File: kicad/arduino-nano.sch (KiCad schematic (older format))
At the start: 28 parts, among them J4 USB_B, J5 AVR ISP, SW5 Reset, U4 CH340C, U5 ATmega328P-AU, Y1 16MHz

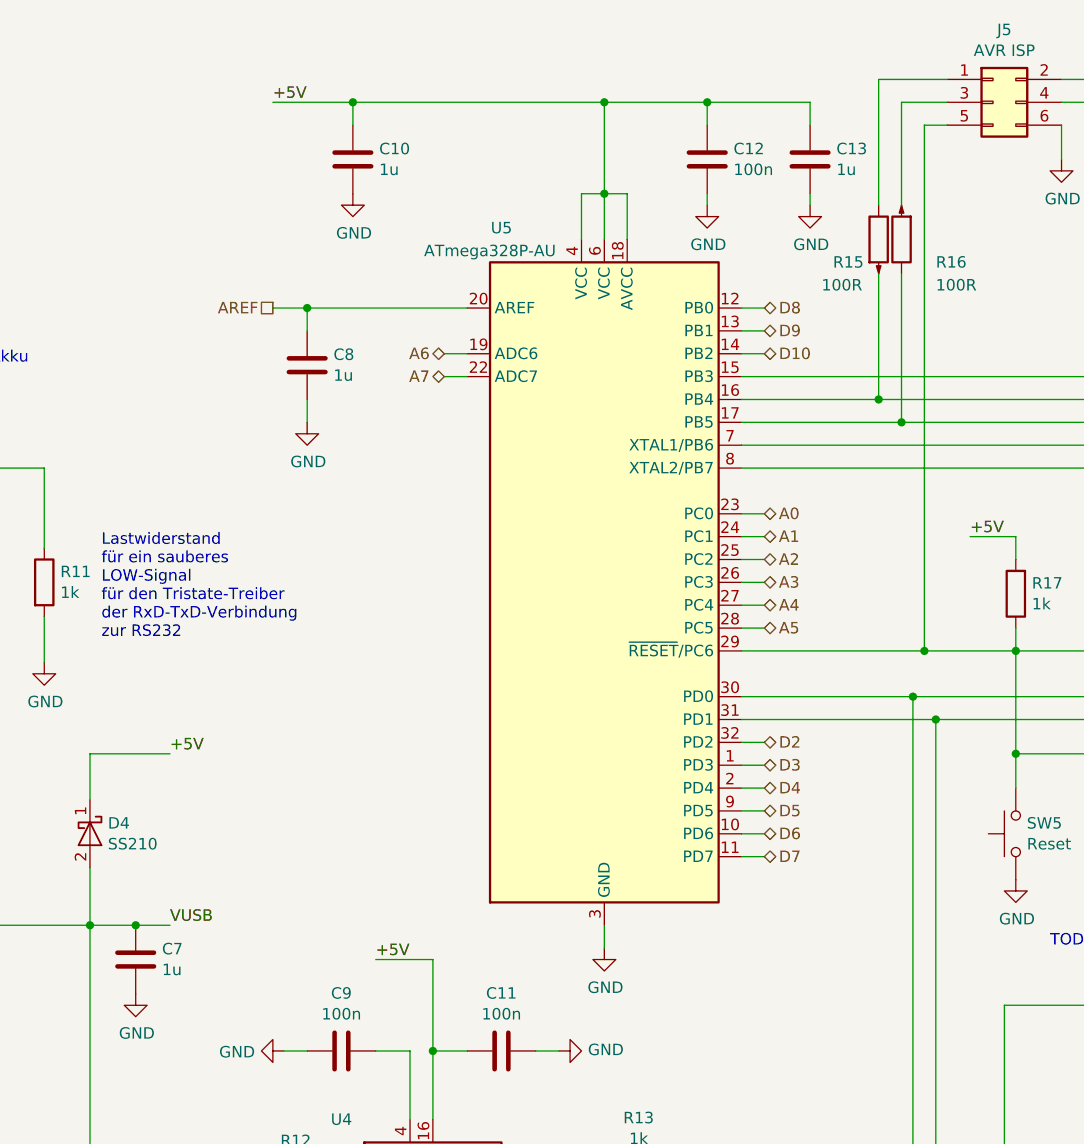
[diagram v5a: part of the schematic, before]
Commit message: wip, bugfixes für v21.0.1
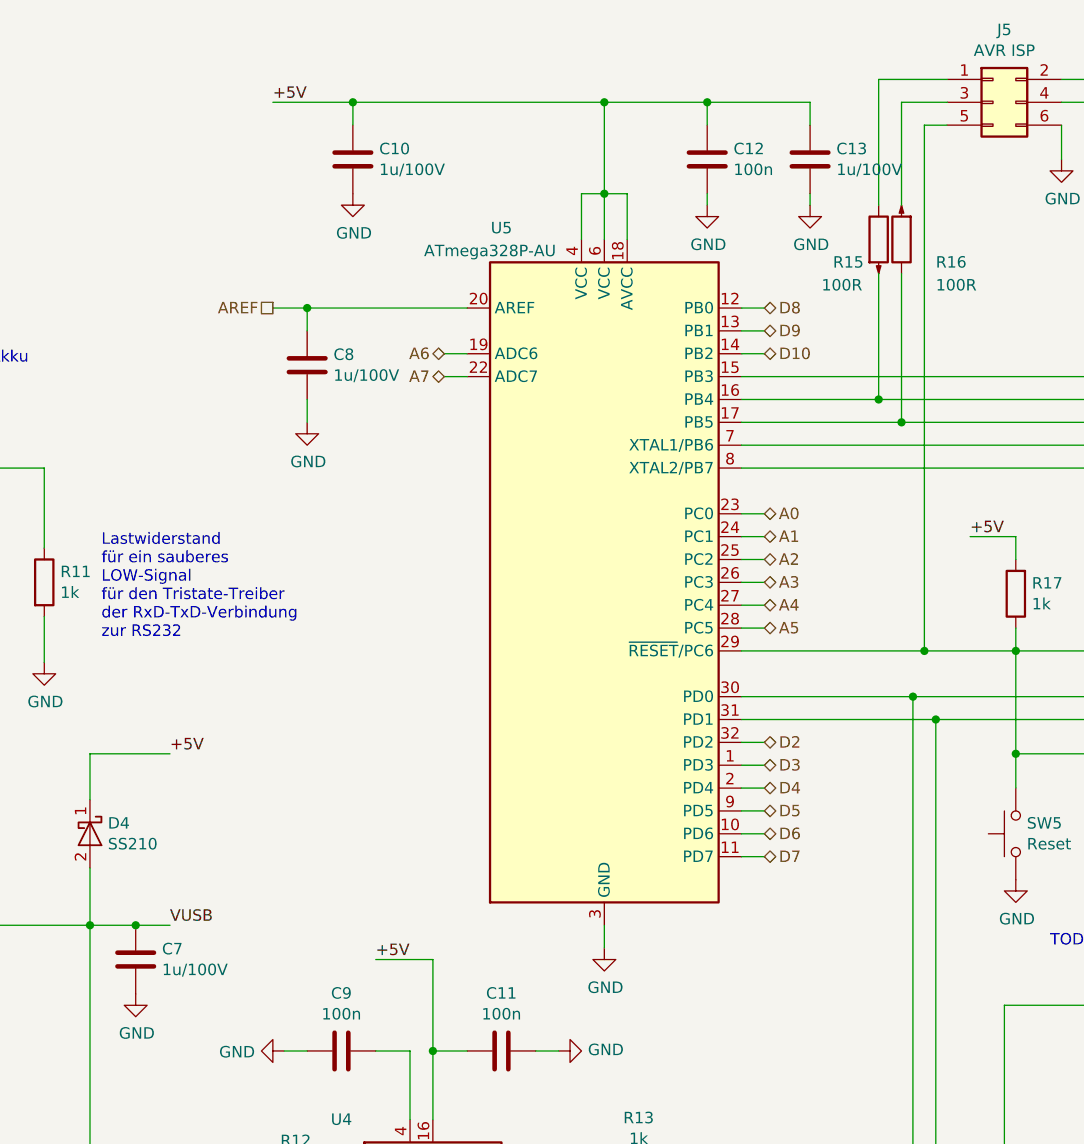
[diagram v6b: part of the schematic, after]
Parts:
- C10, C13, C7, C8: value 1u -> 1u/100V; DistOrderNr C1848 -> C70463; ManPartNr CL31B105KBHNNNE -> CC1206KKX7R0BB105; Manufacturer Samsung -> YAGEO; Notes 1uF ±10% 50V X7R Multilayer Ceramic Capacitors MLCC -> X7R ±10% 100V 1uF 1206 Multilayer Ceramic Capacitors MLCC; PriceEUR 0.0225 -> 0.0535; PriceForQty 100 -> 50; Weblink (none) -> https://www.lcsc.com/product-detail/Multilayer-Ceramic-Capa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
- R12, R14, R15, R16, R18: DistOrderNr C113307 -> C245445; ManPartNr RC1206JR-07100RL -> CR1206F100RP05Z; Manufacturer YAGEO -> Ever Ohms Tech; Notes 100Ω ±5% 0.25W ±100ppm/℃ 1206 Chip Resistor -> 0.25W ±1% ±100ppm/℃ 100Ω 1206; PriceEUR 0.0037 -> 0.0030
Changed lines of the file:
@@
 Sheet 3 10
 Title "HTL Lötregler Mini"
-Date "2021-06-01"
-Rev "21.0.0"
+Date "2021-09-22"
+Rev "21.0.1-dev"
 Comp "HTL Steyr"
 Comment1 "Prof. Karl Zeilhofer et al."
@@
 F 2 "Resistor_SMD:R_1206_3216Metric" V 3080 6100 50  0001 C CNN
 F 3 "https://datasheet.lcsc.com/szlcsc/Uniroyal-Elec-0603WAJ0101T5E_C25201.pdf" H 3150 6100 50  0001 C CNN
-F 4 "C113307" H 3150 6100 50  0001 C CNN "DistOrderNr"
+F 4 "C245445" H 3150 6100 50  0001 C CNN "DistOrderNr"
 F 5 "LCSC" H 3150 6100 50  0001 C CNN "Distributor"
-F 6 "RC1206JR-07100RL" H 3150 6100 50  0001 C CNN "ManPartNr"
-F 7 "YAGEO" H 3150 6100 50  0001 C CNN "Manufacturer"
-F 8 "100Ω ±5% 0.25W ±100ppm/℃ 1206 Chip Resistor" H 3150 6100 50  0001 C CNN "Notes"
-F 9 "0.0037" H 3150 6100 50  0001 C CNN "PriceEUR"
+F 6 "CR1206F100RP05Z" H 3150 6100 50  0001 C CNN "ManPartNr"
+F 7 "Ever Ohms Tech" H 3150 6100 50  0001 C CNN "Manufacturer"
+F 8 "0.25W ±1% ±100ppm/℃ 100Ω 1206" H 3150 6100 50  0001 C CNN "Notes"
+F 9 "0.0030" H 3150 6100 50  0001 C CNN "PriceEUR"
 F 10 "500" H 3150 6100 50  0001 C CNN "PriceForQty"
 F 11 "https://lcsc.com/product-detail/Chip-Resistor-Surface-Mount_UNI-ROYAL-Uniroyal-Elec-0603WAJ0101T5E_C25201.html" H 3150 6100 50  0001 C CNN "Weblink"
@@
 F 2 "Resistor_SMD:R_1206_3216Metric" V 4580 6100 50  0001 C CNN
 F 3 "" H 4650 6100 50  0001 C CNN
-F 4 "C113307" H 4650 6100 50  0001 C CNN "DistOrderNr"
+F 4 "C245445" H 4650 6100 50  0001 C CNN "DistOrderNr"
 F 5 "LCSC" H 4650 6100 50  0001 C CNN "Distributor"
-F 6 "RC1206JR-07100RL" H 4650 6100 50  0001 C CNN "ManPartNr"
-F 7 "YAGEO" H 4650 6100 50  0001 C CNN "Manufacturer"
-F 8 "100Ω ±5% 0.25W ±100ppm/℃ 1206 Chip Resistor" H 4650 6100 50  0001 C CNN "Notes"
-F 9 "0.0037" H 4650 6100 50  0001 C CNN "PriceEUR"
+F 6 "CR1206F100RP05Z" H 4650 6100 50  0001 C CNN "ManPartNr"
+F 7 "Ever Ohms Tech" H 4650 6100 50  0001 C CNN "Manufacturer"
+F 8 "0.25W ±1% ±100ppm/℃ 100Ω 1206" H 4650 6100 50  0001 C CNN "Notes"
+F 9 "0.0030" H 4650 6100 50  0001 C CNN "PriceEUR"
 F 10 "500" H 4650 6100 50  0001 C CNN "PriceForQty"
 	1    4650 6100
@@
 AR Path="/608DBC3C/60930C19/609F24D5" Ref="C7"  Part="1"
 F 0 "C7" H 2565 5146 50  0000 L CNN
-F 1 "1u" H 2565 5055 50  0000 L CNN
+F 1 "1u/100V" H 2565 5055 50  0000 L CNN
 F 2 "Capacitor_SMD:C_1206_3216Metric" H 2488 4950 50  0001 C CNN
 F 3 "~" H 2450 5100 50  0001 C CNN
-F 4 "C1848" H 2450 5100 50  0001 C CNN "DistOrderNr"
+F 4 "C70463" H 2450 5100 50  0001 C CNN "DistOrderNr"
 F 5 "LCSC" H 2450 5100 50  0001 C CNN "Distributor"
-F 6 "CL31B105KBHNNNE" H 2450 5100 50  0001 C CNN "ManPartNr"
-F 7 "Samsung" H 2450 5100 50  0001 C CNN "Manufacturer"
-F 8 "1uF ±10% 50V X7R Multilayer Ceramic Capacitors MLCC" H 2450 5100 50  0001 C CNN "Notes"
-F 9 "0.0225" H 2450 5100 50  0001 C CNN "PriceEUR"
-F 10 "100" H 2450 5100 50  0001 C CNN "PriceForQty"
+F 6 "CC1206KKX7R0BB105" H 2450 5100 50  0001 C CNN "ManPartNr"
+F 7 "YAGEO" H 2450 5100 50  0001 C CNN "Manufacturer"
+F 8 "X7R ±10% 100V 1uF 1206 Multilayer Ceramic Capacitors MLCC" H 2450 5100 50  0001 C CNN "Notes"
+F 9 "0.0535 " H 2450 5100 50  0001 C CNN "PriceEUR"
+F 10 "50" H 2450 5100 50  0001 C CNN "PriceForQty"
+F 11 "https://www.lcsc.com/product-detail/Multilayer-Ceramic-Capacitors-MLCC-SMD-SMT_HUI-JU-NC1206B105K101CEPN_C710469.html" H 2450 5100 50  0001 C CNN "Weblink"
 	1    2450 5100
 	1    0    0    -1
@@
 AR Path="/608DBC3C/60930C19/609FC0C3" Ref="C8"  Part="1"
 F 0 "C8" H 3315 2546 50  0000 L CNN
-F 1 "1u" H 3315 2455 50  0000 L CNN
+F 1 "1u/100V" H 3315 2455 50  0000 L CNN
 F 2 "Capacitor_SMD:C_1206_3216Metric" H 3238 2350 50  0001 C CNN
 F 3 "~" H 3200 2500 50  0001 C CNN
-F 4 "C1848" H 3200 2500 50  0001 C CNN "DistOrderNr"
+F 4 "C70463" H 3200 2500 50  0001 C CNN "DistOrderNr"
 F 5 "LCSC" H 3200 2500 50  0001 C CNN "Distributor"
-F 6 "CL31B105KBHNNNE" H 3200 2500 50  0001 C CNN "ManPartNr"
-F 7 "Samsung" H 3200 2500 50  0001 C CNN "Manufacturer"
-F 8 "1uF ±10% 50V X7R Multilayer Ceramic Capacitors MLCC" H 3200 2500 50  0001 C CNN "Notes"
-F 9 "0.0225" H 3200 2500 50  0001 C CNN "PriceEUR"
-F 10 "100" H 3200 2500 50  0001 C CNN "PriceForQty"
+F 6 "CC1206KKX7R0BB105" H 3200 2500 50  0001 C CNN "ManPartNr"
+F 7 "YAGEO" H 3200 2500 50  0001 C CNN "Manufacturer"
+F 8 "X7R ±10% 100V 1uF 1206 Multilayer Ceramic Capacitors MLCC" H 3200 2500 50  0001 C CNN "Notes"
+F 9 "0.0535 " H 3200 2500 50  0001 C CNN "PriceEUR"
+F 10 "50" H 3200 2500 50  0001 C CNN "PriceForQty"
+F 11 "https://www.lcsc.com/product-detail/Multilayer-Ceramic-Capacitors-MLCC-SMD-SMT_HUI-JU-NC1206B105K101CEPN_C710469.html" H 3200 2500 50  0001 C CNN "Weblink"
 	1    3200 2500
 	1    0    0    -1
@@
 AR Path="/608DBC3C/60930C19/60A0343E" Ref="C13"  Part="1"
 F 0 "C13" H 5515 1646 50  0000 L CNN
-F 1 "1u" H 5515 1555 50  0000 L CNN
+F 1 "1u/100V" H 5515 1555 50  0000 L CNN
 F 2 "Capacitor_SMD:C_1206_3216Metric" H 5438 1450 50  0001 C CNN
 F 3 "~" H 5400 1600 50  0001 C CNN
-F 4 "C1848" H 5400 1600 50  0001 C CNN "DistOrderNr"
+F 4 "C70463" H 5400 1600 50  0001 C CNN "DistOrderNr"
 F 5 "LCSC" H 5400 1600 50  0001 C CNN "Distributor"
-F 6 "CL31B105KBHNNNE" H 5400 1600 50  0001 C CNN "ManPartNr"
-F 7 "Samsung" H 5400 1600 50  0001 C CNN "Manufacturer"
-F 8 "1uF ±10% 50V X7R Multilayer Ceramic Capacitors MLCC" H 5400 1600 50  0001 C CNN "Notes"
-F 9 "0.0225" H 5400 1600 50  0001 C CNN "PriceEUR"
-F 10 "100" H 5400 1600 50  0001 C CNN "PriceForQty"
+F 6 "CC1206KKX7R0BB105" H 5400 1600 50  0001 C CNN "ManPartNr"
+F 7 "YAGEO" H 5400 1600 50  0001 C CNN "Manufacturer"
+F 8 "X7R ±10% 100V 1uF 1206 Multilayer Ceramic Capacitors MLCC" H 5400 1600 50  0001 C CNN "Notes"
+F 9 "0.0535 " H 5400 1600 50  0001 C CNN "PriceEUR"
+F 10 "50" H 5400 1600 50  0001 C CNN "PriceForQty"
+F 11 "https://www.lcsc.com/product-detail/Multilayer-Ceramic-Capacitors-MLCC-SMD-SMT_HUI-JU-NC1206B105K101CEPN_C710469.html" H 5400 1600 50  0001 C CNN "Weblink"
 	1    5400 1600
 	1    0    0    -1
@@
 F 2 "Resistor_SMD:R_1206_3216Metric" V 5730 1950 50  0001 C CNN
 F 3 "" H 5800 1950 50  0001 C CNN
-F 4 "C113307" H 5800 1950 50  0001 C CNN "DistOrderNr"
+F 4 "C245445" H 5800 1950 50  0001 C CNN "DistOrderNr"
 F 5 "LCSC" H 5800 1950 50  0001 C CNN "Distributor"
-F 6 "RC1206JR-07100RL" H 5800 1950 50  0001 C CNN "ManPartNr"
-F 7 "YAGEO" H 5800 1950 50  0001 C CNN "Manufacturer"
-F 8 "100Ω ±5% 0.25W ±100ppm/℃ 1206 Chip Resistor" H 5800 1950 50  0001 C CNN "Notes"
-F 9 "0.0037" H 5800 1950 50  0001 C CNN "PriceEUR"
+F 6 "CR1206F100RP05Z" H 5800 1950 50  0001 C CNN "ManPartNr"
+F 7 "Ever Ohms Tech" H 5800 1950 50  0001 C CNN "Manufacturer"
+F 8 "0.25W ±1% ±100ppm/℃ 100Ω 1206" H 5800 1950 50  0001 C CNN "Notes"
+F 9 "0.0030" H 5800 1950 50  0001 C CNN "PriceEUR"
 F 10 "500" H 5800 1950 50  0001 C CNN "PriceForQty"
 	1    5800 1950
@@
 F 2 "Resistor_SMD:R_1206_3216Metric" V 5630 1950 50  0001 C CNN
 F 3 "" H 5700 1950 50  0001 C CNN
-F 4 "C113307" H 5700 1950 50  0001 C CNN "DistOrderNr"
+F 4 "C245445" H 5700 1950 50  0001 C CNN "DistOrderNr"
 F 5 "LCSC" H 5700 1950 50  0001 C CNN "Distributor"
-F 6 "RC1206JR-07100RL" H 5700 1950 50  0001 C CNN "ManPartNr"
-F 7 "YAGEO" H 5700 1950 50  0001 C CNN "Manufacturer"
-F 8 "100Ω ±5% 0.25W ±100ppm/℃ 1206 Chip Resistor" H 5700 1950 50  0001 C CNN "Notes"
-F 9 "0.0037" H 5700 1950 50  0001 C CNN "PriceEUR"
+F 6 "CR1206F100RP05Z" H 5700 1950 50  0001 C CNN "ManPartNr"
+F 7 "Ever Ohms Tech" H 5700 1950 50  0001 C CNN "Manufacturer"
+F 8 "0.25W ±1% ±100ppm/℃ 100Ω 1206" H 5700 1950 50  0001 C CNN "Notes"
+F 9 "0.0030" H 5700 1950 50  0001 C CNN "PriceEUR"
 F 10 "500" H 5700 1950 50  0001 C CNN "PriceForQty"
 	1    5700 1950
@@
 F 2 "Resistor_SMD:R_1206_3216Metric" V 6580 1950 50  0001 C CNN
 F 3 "" H 6650 1950 50  0001 C CNN
-F 4 "C113307" H 6650 1950 50  0001 C CNN "DistOrderNr"
+F 4 "C245445" H 6650 1950 50  0001 C CNN "DistOrderNr"
 F 5 "LCSC" H 6650 1950 50  0001 C CNN "Distributor"
-F 6 "RC1206JR-07100RL" H 6650 1950 50  0001 C CNN "ManPartNr"
-F 7 "YAGEO" H 6650 1950 50  0001 C CNN "Manufacturer"
-F 8 "100Ω ±5% 0.25W ±100ppm/℃ 1206 Chip Resistor" H 6650 1950 50  0001 C CNN "Notes"
-F 9 "0.0037" H 6650 1950 50  0001 C CNN "PriceEUR"
+F 6 "CR1206F100RP05Z" H 6650 1950 50  0001 C CNN "ManPartNr"
+F 7 "Ever Ohms Tech" H 6650 1950 50  0001 C CNN "Manufacturer"
+F 8 "0.25W ±1% ±100ppm/℃ 100Ω 1206" H 6650 1950 50  0001 C CNN "Notes"
+F 9 "0.0030" H 6650 1950 50  0001 C CNN "PriceEUR"
 F 10 "500" H 6650 1950 50  0001 C CNN "PriceForQty"
 	1    6650 1950
@@
 AR Path="/608DBC3C/60930C19/60B0FAED" Ref="C10"  Part="1"
 F 0 "C10" H 3515 1646 50  0000 L CNN
-F 1 "1u" H 3515 1555 50  0000 L CNN
+F 1 "1u/100V" H 3515 1555 50  0000 L CNN
 F 2 "Capacitor_SMD:C_1206_3216Metric" H 3438 1450 50  0001 C CNN
 F 3 "~" H 3400 1600 50  0001 C CNN
-F 4 "C1848" H 3400 1600 50  0001 C CNN "DistOrderNr"
+F 4 "C70463" H 3400 1600 50  0001 C CNN "DistOrderNr"
 F 5 "LCSC" H 3400 1600 50  0001 C CNN "Distributor"
-F 6 "CL31B105KBHNNNE" H 3400 1600 50  0001 C CNN "ManPartNr"
-F 7 "Samsung" H 3400 1600 50  0001 C CNN "Manufacturer"
-F 8 "1uF ±10% 50V X7R Multilayer Ceramic Capacitors MLCC" H 3400 1600 50  0001 C CNN "Notes"
-F 9 "0.0225" H 3400 1600 50  0001 C CNN "PriceEUR"
-F 10 "100" H 3400 1600 50  0001 C CNN "PriceForQty"
+F 6 "CC1206KKX7R0BB105" H 3400 1600 50  0001 C CNN "ManPartNr"
+F 7 "YAGEO" H 3400 1600 50  0001 C CNN "Manufacturer"
+F 8 "X7R ±10% 100V 1uF 1206 Multilayer Ceramic Capacitors MLCC" H 3400 1600 50  0001 C CNN "Notes"
+F 9 "0.0535 " H 3400 1600 50  0001 C CNN "PriceEUR"
+F 10 "50" H 3400 1600 50  0001 C CNN "PriceForQty"
+F 11 "https://www.lcsc.com/product-detail/Multilayer-Ceramic-Capacitors-MLCC-SMD-SMT_HUI-JU-NC1206B105K101CEPN_C710469.html" H 3400 1600 50  0001 C CNN "Weblink"
 	1    3400 1600
 	1    0    0    -1

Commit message: BOM aktualisiert, Zenerdiode: Pinout IPC-konform gestaltet, ...
siehe https://gitlab.com/kicad/libraries/kicad-symbols/-/issues/3157
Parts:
- C10, C13, C7, C8: Index (none) -> 10
- C11, C12, C14, C9: Index (none) -> 40
- C15, C16: Index (none) -> 13
- C38: Index (none) -> 44
- D3: Index (none) -> 47
- D4: Index (none) -> 49
- J4: Index (none) -> 6
- J5: Index (none) -> 16
- R10: Index (none) -> 26
- R11, R13, R17: Index (none) -> 12
- R12, R14, R15, R16, R18: Index (none) -> 28
- SW5: Index (none) -> 33
- U4: Index (none) -> 11
- U5: Index (none) -> 1; NotesAlt (none) -> https://www.reichelt.at/at/de/8-bit-atmega-avr-mikrocontrol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
- Y1: Index (none) -> 35
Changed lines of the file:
@@
 F 12 "C464972" H 4050 5500 50  0001 C CNN "DistOrderNr"
 F 13 "FN31X104K500PXG" H 4050 5500 50  0001 C CNN "ManPartNr"
+F 14 "40" H 4050 5500 50  0001 C CNN "Index"
+F 15 "" H 4050 5500 50  0001 C CNN "NotesAlt"
 	1    4050 5500
 	0    1    1    0
@@
 F 10 "CH340C" H 3750 6400 50  0001 C CNN "ManPartNr"
 F 11 "USB-UART with internal clock" H 3750 6400 50  0001 C CNN "Notes"
+F 12 "11" H 3750 6400 50  0001 C CNN "Index"
 	1    3750 6400
 	1    0    0    -1
@@
 F 10 "500" H 3150 6100 50  0001 C CNN "PriceForQty"
 F 11 "https://lcsc.com/product-detail/Chip-Resistor-Surface-Mount_UNI-ROYAL-Uniroyal-Elec-0603WAJ0101T5E_C25201.html" H 3150 6100 50  0001 C CNN "Weblink"
+F 12 "28" H 3150 6100 50  0001 C CNN "Index"
 	1    3150 6100
 	0    1    1    0
@@
 F 12 "C464972" H 3350 5500 50  0001 C CNN "DistOrderNr"
 F 13 "FN31X104K500PXG" H 3350 5500 50  0001 C CNN "ManPartNr"
+F 14 "40" H 3350 5500 50  0001 C CNN "Index"
+F 15 "" H 3350 5500 50  0001 C CNN "NotesAlt"
 	1    3350 5500
 	0    1    1    0
@@
 F 9 "0.0042" H 4650 6000 50  0001 C CNN "PriceEUR"
 F 10 "50" H 4650 6000 50  0001 C CNN "PriceForQty"
+F 11 "12" H 4650 6000 50  0001 C CNN "Index"
 	1    4650 6000
 	0    -1   -1   0
@@
 F 9 "0.0030" H 4650 6100 50  0001 C CNN "PriceEUR"
 F 10 "500" H 4650 6100 50  0001 C CNN "PriceForQty"
+F 11 "28" H 4650 6100 50  0001 C CNN "Index"
 	1    4650 6100
 	0    1    1    0
@@
 F 9 "1.0" H 4500 3450 50  0001 C CNN "PriceEUR"
 F 10 "1" H 4500 3450 50  0001 C CNN "PriceForQty"
+F 11 "1" H 4500 3450 50  0001 C CNN "Index"
+F 12 "https://www.reichelt.at/at/de/8-bit-atmega-avr-mikrocontroller-32kb-20-mhz-tqfp-32-gegurtet-atmega-328p-aur-p269066.html" H 4500 3450 50  0001 C CNN "NotesAlt"
 	1    4500 3450
 	1    0    0    -1
@@
 F 10 "50" H 6300 3500 50  0001 C CNN "PriceForQty"
 F 11 "https://lcsc.com/product-detail/Chip-Resistor-Surface-Mount_UNI-ROYAL-Uniroyal-Elec-0603WAJ0101T5E_C25201.html" H 6300 3500 50  0001 C CNN "Weblink"
+F 12 "12" H 6300 3500 50  0001 C CNN "Index"
 	1    6300 3500
 	-1   0    0    1
@@
 F 9 "0.0155" H 2250 4550 50  0001 C CNN "PriceEUR"
 F 10 "200" H 2250 4550 50  0001 C CNN "PriceForQty"
+F 11 "49" H 2250 4550 50  0001 C CNN "Index"
 	1    2250 4550
 	0    1    1    0
@@
 F 9 "0.0777" H 1550 6300 50  0001 C CNN "PriceEUR"
 F 10 "5" H 1550 6300 50  0001 C CNN "PriceForQty"
+F 11 "6" H 1550 6300 50  0001 C CNN "Index"
 	1    1550 6300
 	1    0    0    -1
@@
 F 12 "C464972" H 7200 4550 50  0001 C CNN "DistOrderNr"
 F 13 "FN31X104K500PXG" H 7200 4550 50  0001 C CNN "ManPartNr"
+F 14 "40" H 7200 4550 50  0001 C CNN "Index"
+F 15 "" H 7200 4550 50  0001 C CNN "NotesAlt"
 	1    7200 4550
 	-1   0    0    1
@@
 F 9 "0.0884" H 7950 2900 50  0001 C CNN "PriceEUR"
 F 10 "50" H 7950 2900 50  0001 C CNN "PriceForQty"
+F 11 "35" H 7950 2900 50  0001 C CNN "Index"
 	1    7950 2900
 	0    -1   -1   0
@@
 F 9 "0.024" H 8200 3200 50  0001 C CNN "PriceEUR"
 F 10 "20" H 8200 3200 50  0001 C CNN "PriceForQty"
+F 11 "13" H 8200 3200 50  0001 C CNN "Index"
 	1    8200 3200
 	0    -1   -1   0
@@
 F 9 "0.024" H 8200 2350 50  0001 C CNN "PriceEUR"
 F 10 "20" H 8200 2350 50  0001 C CNN "PriceForQty"
+F 11 "13" H 8200 2350 50  0001 C CNN "Index"
 	1    8200 2350
 	0    -1   -1   0
@@
 F 10 "500" H 6300 4550 50  0001 C CNN "PriceForQty"
 F 11 "https://lcsc.com/product-detail/Tactile-Switches_XKB-Connectivity-TS-1187A-B-A-B_C318884.html" H 6300 4550 50  0001 C CNN "Weblink"
+F 12 "33" H 6300 4550 50  0001 C CNN "Index"
 	1    6300 4550
 	0    -1   -1   0
@@
 F 12 "C464972" H 4950 1600 50  0001 C CNN "DistOrderNr"
 F 13 "FN31X104K500PXG" H 4950 1600 50  0001 C CNN "ManPartNr"
+F 14 "40" H 4950 1600 50  0001 C CNN "Index"
+F 15 "" H 4950 1600 50  0001 C CNN "NotesAlt"
 	1    4950 1600
 	-1   0    0    1
@@
 F 5 "C229599" H 1550 3150 50  0001 C CNN "DistOrderNr"
 F 6 "LCSC" H 1550 3150 50  0001 C CNN "Distributor"
+F 7 "26" H 1550 3150 50  0001 C CNN "Index"
 	1    1550 3150
 	1    0    0    -1
@@
 F 7 "0.0067" H 1550 3550 50  0001 C CNN "PriceEUR"
 F 8 "50" H 1550 3550 50  0001 C CNN "PriceForQty"
+F 9 "47" H 1550 3550 50  0001 C CNN "Index"
 	1    1550 3550
 	0    -1   -1   0
@@
 F 9 "1kΩ ±5% 0.25W ±100ppm/℃ 1206 Chip Resistor" H 2050 3450 50  0001 C CNN "Notes"
 F 10 "50" H 2050 3450 50  0001 C CNN "PriceForQty"
+F 11 "12" H 2050 3450 50  0001 C CNN "Index"
 	1    2050 3450
 	1    0    0    -1
@@
 F 10 "50" H 2450 5100 50  0001 C CNN "PriceForQty"
 F 11 "https://www.lcsc.com/product-detail/Multilayer-Ceramic-Capacitors-MLCC-SMD-SMT_HUI-JU-NC1206B105K101CEPN_C710469.html" H 2450 5100 50  0001 C CNN "Weblink"
+F 12 "10" H 2450 5100 50  0001 C CNN "Index"
 	1    2450 5100
 	1    0    0    -1
@@
 F 10 "50" H 3200 2500 50  0001 C CNN "PriceForQty"
 F 11 "https://www.lcsc.com/product-detail/Multilayer-Ceramic-Capacitors-MLCC-SMD-SMT_HUI-JU-NC1206B105K101CEPN_C710469.html" H 3200 2500 50  0001 C CNN "Weblink"
+F 12 "10" H 3200 2500 50  0001 C CNN "Index"
 	1    3200 2500
 	1    0    0    -1
@@
 F 10 "50" H 5400 1600 50  0001 C CNN "PriceForQty"
 F 11 "https://www.lcsc.com/product-detail/Multilayer-Ceramic-Capacitors-MLCC-SMD-SMT_HUI-JU-NC1206B105K101CEPN_C710469.html" H 5400 1600 50  0001 C CNN "Weblink"
+F 12 "10" H 5400 1600 50  0001 C CNN "Index"
 	1    5400 1600
 	1    0    0    -1
@@
 F 7 "0.0698" H 6200 1350 50  0001 C CNN "PriceEUR"
 F 8 "50" H 6200 1350 50  0001 C CNN "PriceForQty"
+F 9 "16" H 6200 1350 50  0001 C CNN "Index"
 	1    6200 1350
 	1    0    0    -1
@@
 F 9 "0.0030" H 5800 1950 50  0001 C CNN "PriceEUR"
 F 10 "500" H 5800 1950 50  0001 C CNN "PriceForQty"
+F 11 "28" H 5800 1950 50  0001 C CNN "Index"
 	1    5800 1950
 	-1   0    0    1
@@
 F 9 "0.0030" H 5700 1950 50  0001 C CNN "PriceEUR"
 F 10 "500" H 5700 1950 50  0001 C CNN "PriceForQty"
+F 11 "28" H 5700 1950 50  0001 C CNN "Index"
 	1    5700 1950
 	1    0    0    -1
@@
 F 9 "0.0030" H 6650 1950 50  0001 C CNN "PriceEUR"
 F 10 "500" H 6650 1950 50  0001 C CNN "PriceForQty"
+F 11 "28" H 6650 1950 50  0001 C CNN "Index"
 	1    6650 1950
 	-1   0    0    1
@@
 F 10 "50" H 3400 1600 50  0001 C CNN "PriceForQty"
 F 11 "https://www.lcsc.com/product-detail/Multilayer-Ceramic-Capacitors-MLCC-SMD-SMT_HUI-JU-NC1206B105K101CEPN_C710469.html" H 3400 1600 50  0001 C CNN "Weblink"
+F 12 "10" H 3400 1600 50  0001 C CNN "Index"
 	1    3400 1600
 	1    0    0    -1
@@
 F 9 "0.0106" H 6700 4600 50  0001 C CNN "PriceEUR"
 F 10 "500" H 6700 4600 50  0001 C CNN "PriceForQty"
+F 11 "44" H 6700 4600 50  0001 C CNN "Index"
 	1    6700 4600
 	1    0    0    -1
